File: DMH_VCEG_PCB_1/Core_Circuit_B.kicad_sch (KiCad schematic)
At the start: 111 parts, among them J24 Conn_01x06_PinHeader, J25 Conn_01x10_PinHeader, J26 Conn_01x10_PinHeader, J27 Conn_01x10_PinHeader, Q17 BC558, Q18 BC558, Q19 BC548, Q20 BC548, Q21 BS170, Q22 BS170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

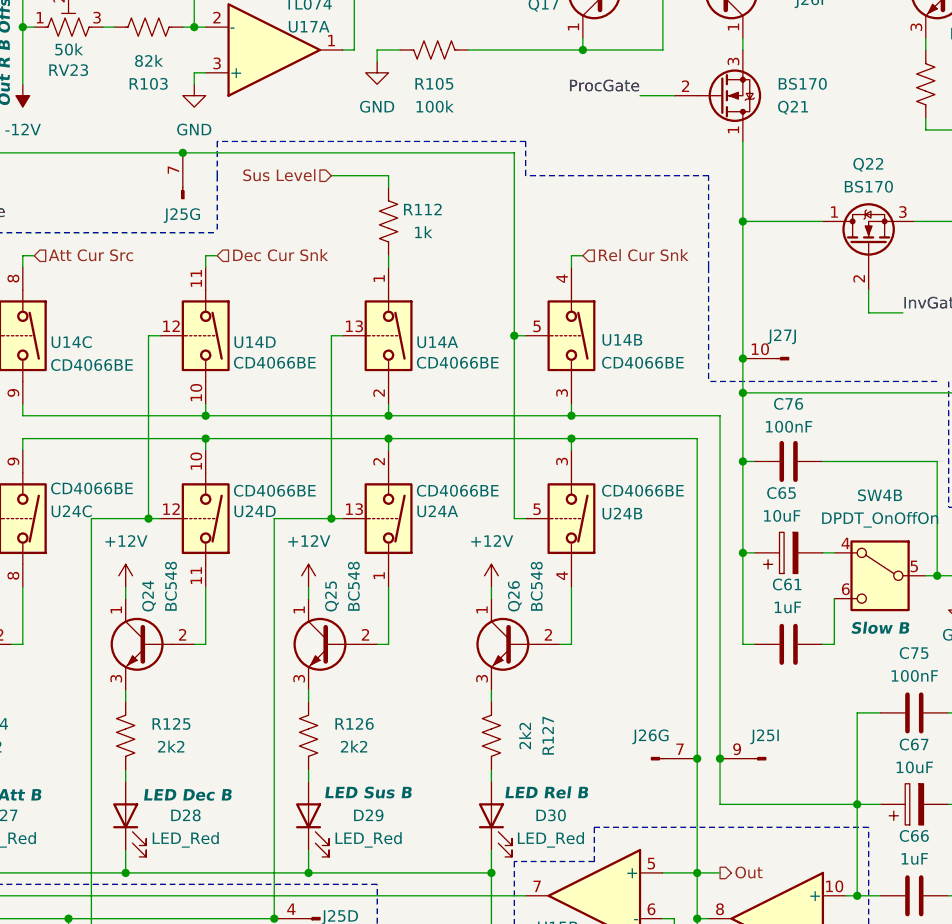
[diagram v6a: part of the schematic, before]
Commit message: PCB 1 placement in progress
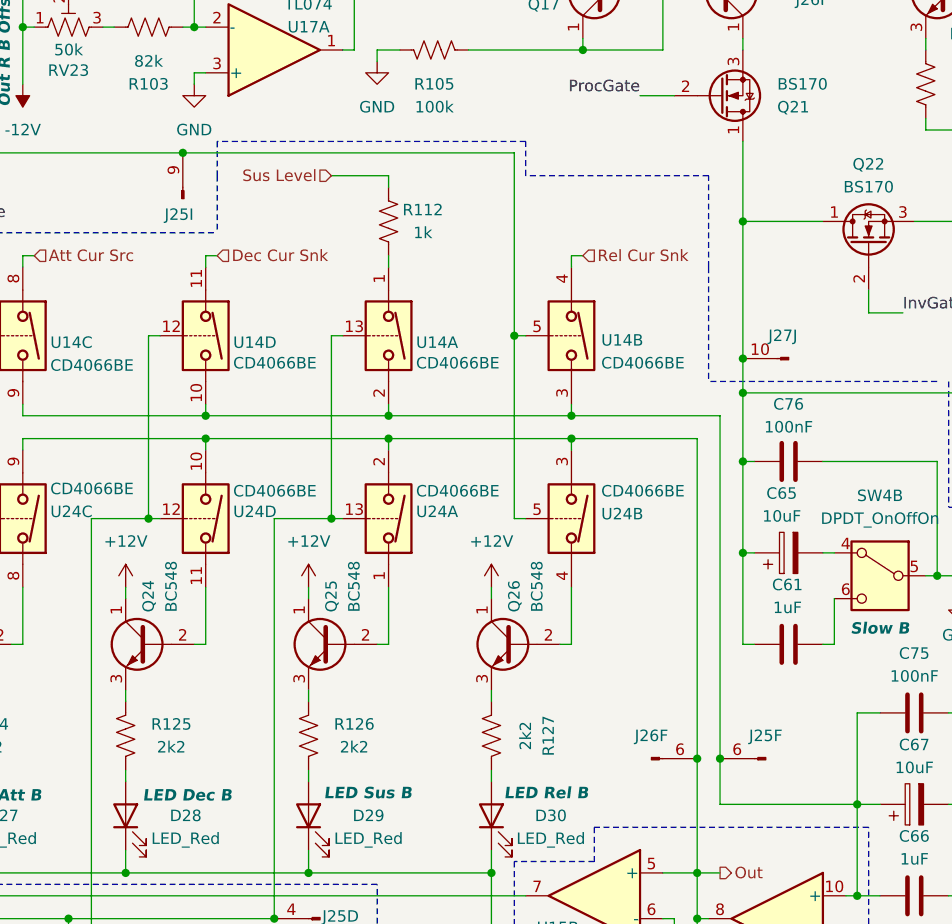
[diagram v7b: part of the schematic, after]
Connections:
- net Out: now also J26.6 (Pin_6); no longer J26.7 (Pin_7)
- net Rel_State: now also J25.9 (Pin_9); no longer J25.7 (Pin_7)
- net at C66.1, C67.1, C75.2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: now also J25.6 (Pin_6); no longer J25.9 (Pin_9)
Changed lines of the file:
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@@
 		(lib_id "SynthStuff:Conn_01x10_PinHeader")
 		(at 179.07 48.26 90)
-		(unit 7)
+		(unit 9)
 		(exclude_from_sim no)
 		(in_bom yes)
@@
 				(path "/58f4306d-5387-4983-bb08-41a2313fd315/8d22a13f-1d3b-4a1f-8b3f-baf42965c019"
 					(reference "J25")
-					(unit 7)
+					(unit 9)
 				)
 			)
@@
 		(lib_id "SynthStuff:Conn_01x10_PinHeader")
 		(at 231.14 110.49 0)
-		(unit 7)
+		(unit 6)
 		(exclude_from_sim no)
 		(in_bom yes)
@@
 				(path "/58f4306d-5387-4983-bb08-41a2313fd315/8d22a13f-1d3b-4a1f-8b3f-baf42965c019"
 					(reference "J26")
-					(unit 7)
+					(unit 6)
 				)
 			)
@@
 		(lib_id "SynthStuff:Conn_01x10_PinHeader")
 		(at 243.84 110.49 180)
-		(unit 9)
+		(unit 6)
 		(exclude_from_sim no)
 		(in_bom yes)
@@
 				(path "/58f4306d-5387-4983-bb08-41a2313fd315/8d22a13f-1d3b-4a1f-8b3f-baf42965c019"
 					(reference "J25")
-					(unit 9)
+					(unit 6)
 				)
 			)

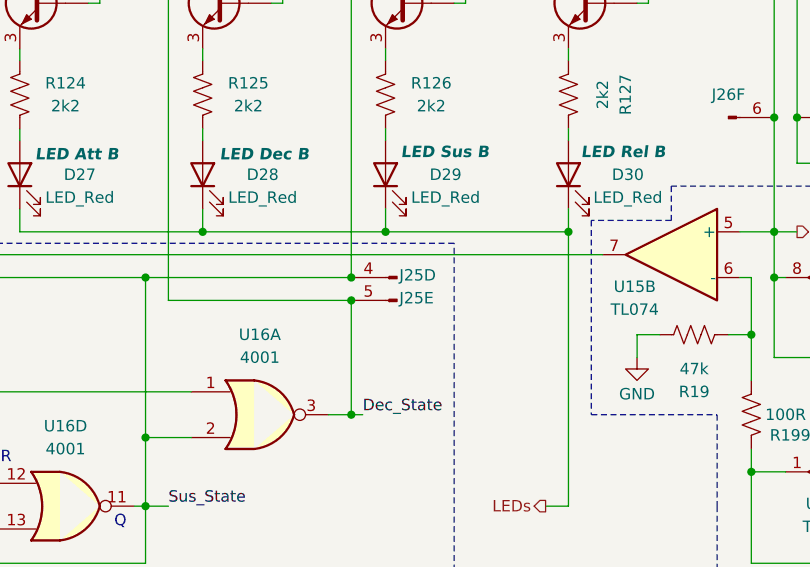
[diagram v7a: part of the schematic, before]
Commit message: PCB 1 placement in progress
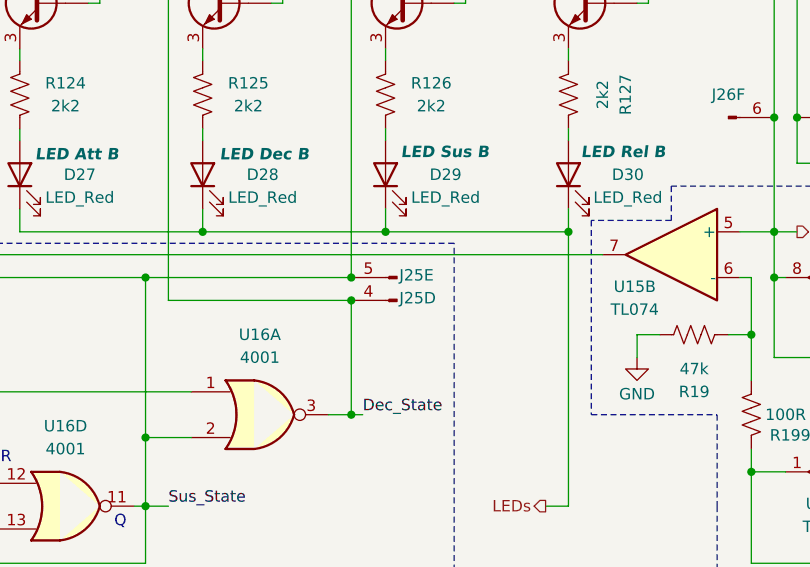
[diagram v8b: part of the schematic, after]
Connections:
- net Dec_State: now also J25.4 (Pin_4); no longer J25.5 (Pin_5)
- net Sus_State: now also J25.5 (Pin_5); no longer J25.4 (Pin_4)
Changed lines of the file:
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@@
 		(lib_id "SynthStuff:Conn_01x10_PinHeader")
 		(at 194.31 130.81 180)
-		(unit 5)
+		(unit 4)
 		(exclude_from_sim no)
 		(in_bom yes)
@@
 				(path "/58f4306d-5387-4983-bb08-41a2313fd315/8d22a13f-1d3b-4a1f-8b3f-baf42965c019"
 					(reference "J25")
-					(unit 5)
+					(unit 4)
 				)
 			)
@@
 		(lib_id "SynthStuff:Conn_01x10_PinHeader")
 		(at 194.31 128.27 180)
-		(unit 4)
+		(unit 5)
 		(exclude_from_sim no)
 		(in_bom yes)
@@
 				(path "/58f4306d-5387-4983-bb08-41a2313fd315/8d22a13f-1d3b-4a1f-8b3f-baf42965c019"
 					(reference "J25")
-					(unit 4)
-				)
-			)
+					(unit 5)
+				)
+			)
